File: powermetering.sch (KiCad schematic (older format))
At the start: 111 parts, among them J1 Conn_01x04, J2 Conn_01x02, J3 Conn_01x02, J4 Conn_01x02, J5 Conn_01x02, U1 ADuM7641, U2 ADE9000, Y1 Crystal

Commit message: repair schematic, change pcb outline to spelsberg tk1111
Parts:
- removed U1: ADuM7641, Housings_SSOP:QSOP-24_3.9x8.7mm_Pitch0.635mm, symbol analog_devices:ADuM7641
- added T1: Transformer_1P_1S, Transformer_THT:Transformer_CHK_EI30-2VA_1xSec, symbol Device:Transformer_1P_1S
- C1, C10, C11, C12, C13, C14, C15, C16, C17, C18, C19, C2, C20, C21, C22, C23, C24, C25, C26, C27, C28, C29, C3, C30, C31, C32, C33, C34, C4, C5, C6, C7, C8, C9: symbol device:C -> stmbl:C
- D1: symbol device:LED -> stmbl:LED
- D10, D11, D12, D13, D14, D15, D16, D17, D2, D3, D4, D5, D6, D7, D8, D9: symbol device:D -> stmbl:D
- F1, F2, F3, F4: symbol device:Fuse -> Device:Fuse
- J1: symbol Connector:Conn_01x04 -> Connector:Conn_01x04_Female
- J2, J3, J4, J5: symbol Connector:Conn_01x02 -> Connector:Conn_01x02_Female
- L1, L2, L3, L4: symbol device:Ferrite_Bead -> Device:Ferrite_Bead
- Y1: symbol device:Crystal -> stmbl:Crystal
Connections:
- net labels added: AVDDOUT, DVDDOUT, IL1N, IL1P, IL2N, IL2P, IL3N, IL3P, INN, INP, REF, UL1N, UL1P, UL2N, UL2P, UL3N, UL3P

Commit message: add stm32, ethernet phy, hv supply with lnk304
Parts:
- added C35, C36: 3.9µ, Capacitor_SMD:CP_Elec_8x10, symbol stmbl:CP
- added C? (x2): 150n, stmbl:C_1808, symbol stmbl:C
- added D18, D19: ABS2, Diode_SMD:Diode_Bridge_Diotec_ABS, symbol Diode_Bridge:ABS2
- added D20, D21: ABS10, Diode_SMD:Diode_Bridge_Diotec_ABS, symbol Diode_Bridge:ABS10
- added D22: 1.5KExxA, Diode_THT:D_DO-201AE_P15.24mm_Horizontal, symbol Diode:1.5KExxA
- added H1, H2, H3, H4, H5, H6, H7, H8: MountingHole_Pad, MountingHole:MountingHole_3.2mm_M3_DIN965_Pad, symbol Mechanical:MountingHole_Pad
- added R45, R46: 450k, stmbl:R_1206, symbol stmbl:R
- added RV1: Varistor, symbol Device:Varistor
- added T2, T3: Transformer_1P_1S, Transformer_THT:Transformer_CHK_EI30-2VA_1xSec, symbol powermetering:Transformer_1P_1S
- F1, F2, F3, F4: footprint Fuse_Holders_and_Fuses:Fuseholder6x32_Horiz_Open_Schurter0031-8002 -> Fuse:Fuse_2920_7451Metric
- R1, R10, R11, R12, R13, R14, R15, R16, R17, R18, R19, R2, R20, R21, R22, R23, R24, R3, R4, R5, R6, R7, R8, R9: footprint Resistors_SMD:R_0603 -> stmbl:R_0603
- R25, R26, R27, R28, R29, R30, R31, R32, R33, R34, R35, R36, R37, R38, R39, R40, R41, R42, R43, R44: footprint Resistors_SMD:R_2010 -> Resistor_SMD:R_2010_5025Metric
- T1: symbol Device:Transformer_1P_1S -> powermetering:Transformer_1P_1S
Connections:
- net labels added: DC+, DC-, GNDPWR, VPP
- wire segments 356 -> 442
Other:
- moved on the sheet: F1, F2, F3, F4, J1, L4

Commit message: remove xfmrs from top board, no space with 18650 backup battery
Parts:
- added BT1: Battery_Cell, Battery:BatteryHolder_Keystone_1042_1x18650, symbol Device:Battery_Cell
- added H10, H11, H12, H13, H14, H15, H16, H9: MountingHole, MountingHole:MountingHole_3.2mm_M3, symbol Mechanical:MountingHole
- gave numbers to parts that had none: 2
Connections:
- net labels added: RESET
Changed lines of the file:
@@
 Wire Wire Line
 	3050 7050 3150 7050
-Text GLabel 15100 2300 2    50   Input ~ 0
+Text GLabel 15100 4400 2    50   Input ~ 0
 L1
 $Comp
@@
 	0    1    1    0
 $EndComp
-Text GLabel 15100 4400 2    50   Input ~ 0
+Text GLabel 15100 2300 2    50   Input ~ 0
 L3
 $Comp
@@
 $EndComp
 Text Label 12550 2550 0    50   ~ 0
-UL1N
+UL3N
 Text Label 13100 2550 0    50   ~ 0
-UL1P
+UL3P
 Text Label 13100 3400 0    50   ~ 0
 UL2P
 Text Label 13100 4300 0    50   ~ 0
-UL3P
+UL1P
 Text Label 12550 3450 0    50   ~ 0
 UL2N
 Text Label 12550 4350 0    50   ~ 0
-UL3N
+UL1N
 Connection ~ 12550 5850
 Wire Wire Line
@@
 	5000 4000 5100 4000
 $Comp
-L stmbl:C C?
+L stmbl:C C63
 U 1 1 5DA79E78
 P 4100 3450
-F 0 "C?" H 4150 3550 50  0000 L CNN
+F 0 "C63" H 4150 3550 50  0000 L CNN
 F 1 "150n" H 4150 3350 50  0000 L CNN
 F 2 "stmbl:C_1808" H 4138 3300 50  0001 C CNN
@@
 	4100 3300 4400 3300
 $Comp
-L stmbl:C C?
+L stmbl:C C73
 U 1 1 5DA7A654
 P 4100 3850
-F 0 "C?" H 4150 3950 50  0000 L CNN
+F 0 "C73" H 4150 3950 50  0000 L CNN
 F 1 "150n" H 4150 3750 50  0000 L CNN
 F 2 "stmbl:C_1808" H 4138 3700 50  0001 C CNN
@@
 Wire Wire Line
 	4100 3650 4100 3700
+Text Label 8400 6800 0    50   ~ 0
+RESET
+$Comp
+L Mechanical:MountingHole H9
+U 1 1 5DBB8804
+P 4500 7850
+F 0 "H9" H 4600 7896 50  0000 L CNN
+F 1 "MountingHole" H 4600 7805 50  0000 L CNN
+F 2 "MountingHole:MountingHole_3.2mm_M3" H 4500 7850 50  0001 C CNN
+F 3 "~" H 4500 7850 50  0001 C CNN
+	1    4500 7850
+	1    0    0    -1
+$EndComp
+$Comp
+L Mechanical:MountingHole H10
+U 1 1 5DBBF11A
+P 4500 8100
+F 0 "H10" H 4600 8146 50  0000 L CNN
+F 1 "MountingHole" H 4600 8055 50  0000 L CNN
+F 2 "MountingHole:MountingHole_3.2mm_M3" H 4500 8100 50  0001 C CNN
+F 3 "~" H 4500 8100 50  0001 C CNN
+	1    4500 8100
+	1    0    0    -1
+$EndComp
+$Comp
+L Mechanical:MountingHole H11
+U 1 1 5DBBF269
+P 4500 8350
+F 0 "H11" H 4600 8396 50  0000 L CNN
+F 1 "MountingHole" H 4600 8305 50  0000 L CNN
+F 2 "MountingHole:MountingHole_3.2mm_M3" H 4500 8350 50  0001 C CNN
+F 3 "~" H 4500 8350 50  0001 C CNN
+	1    4500 8350
+	1    0    0    -1
+$EndComp
+$Comp
+L Mechanical:MountingHole H12
+U 1 1 5DBBF7A6
+P 4500 8600
+F 0 "H12" H 4600 8646 50  0000 L CNN
+F 1 "MountingHole" H 4600 8555 50  0000 L CNN
+F 2 "MountingHole:MountingHole_3.2mm_M3" H 4500 8600 50  0001 C CNN
+F 3 "~" H 4500 8600 50  0001 C CNN
+	1    4500 8600
+	1    0    0    -1
+$EndComp
+$Comp
+L Mechanical:MountingHole H16
+U 1 1 5DBBF92B
+P 5300 8600
+F 0 "H16" H 5400 8646 50  0000 L CNN
+F 1 "MountingHole" H 5400 8555 50  0000 L CNN
+F 2 "MountingHole:MountingHole_3.2mm_M3" H 5300 8600 50  0001 C CNN
+F 3 "~" H 5300 8600 50  0001 C CNN
+	1    5300 8600
+	1    0    0    -1
+$EndComp
+$Comp
+L Mechanical:MountingHole H15
+U 1 1 5DBBFB1F
+P 5300 8350
+F 0 "H15" H 5400 8396 50  0000 L CNN
+F 1 "MountingHole" H 5400 8305 50  0000 L CNN
+F 2 "MountingHole:MountingHole_3.2mm_M3" H 5300 8350 50  0001 C CNN
+F 3 "~" H 5300 8350 50  0001 C CNN
+	1    5300 8350
+	1    0    0    -1
+$EndComp
+$Comp
+L Mechanical:MountingHole H14
+U 1 1 5DBBFF20
+P 5300 8100
+F 0 "H14" H 5400 8146 50  0000 L CNN
+F 1 "MountingHole" H 5400 8055 50  0000 L CNN
+F 2 "MountingHole:MountingHole_3.2mm_M3" H 5300 8100 50  0001 C CNN
+F 3 "~" H 5300 8100 50  0001 C CNN
+	1    5300 8100
+	1    0    0    -1
+$EndComp
+$Comp
+L Mechanical:MountingHole H13
+U 1 1 5DBC00A9
+P 5300 7850
+F 0 "H13" H 5400 7896 50  0000 L CNN
+F 1 "MountingHole" H 5400 7805 50  0000 L CNN
+F 2 "MountingHole:MountingHole_3.2mm_M3" H 5300 7850 50  0001 C CNN
+F 3 "~" H 5300 7850 50  0001 C CNN
+	1    5300 7850
+	1    0    0    -1
+$EndComp
+$Comp
+L Device:Battery_Cell BT1
+U 1 1 5DBD7F45
+P 1800 5750
+F 0 "BT1" H 1918 5846 50  0000 L CNN
+F 1 "Battery_Cell" H 1918 5755 50  0000 L CNN
+F 2 "Battery:BatteryHolder_Keystone_1042_1x18650" V 1800 5810 50  0001 C CNN
+F 3 "~" V 1800 5810 50  0001 C CNN
+	1    1800 5750
+	1    0    0    -1
+$EndComp
 $EndSCHEMATC

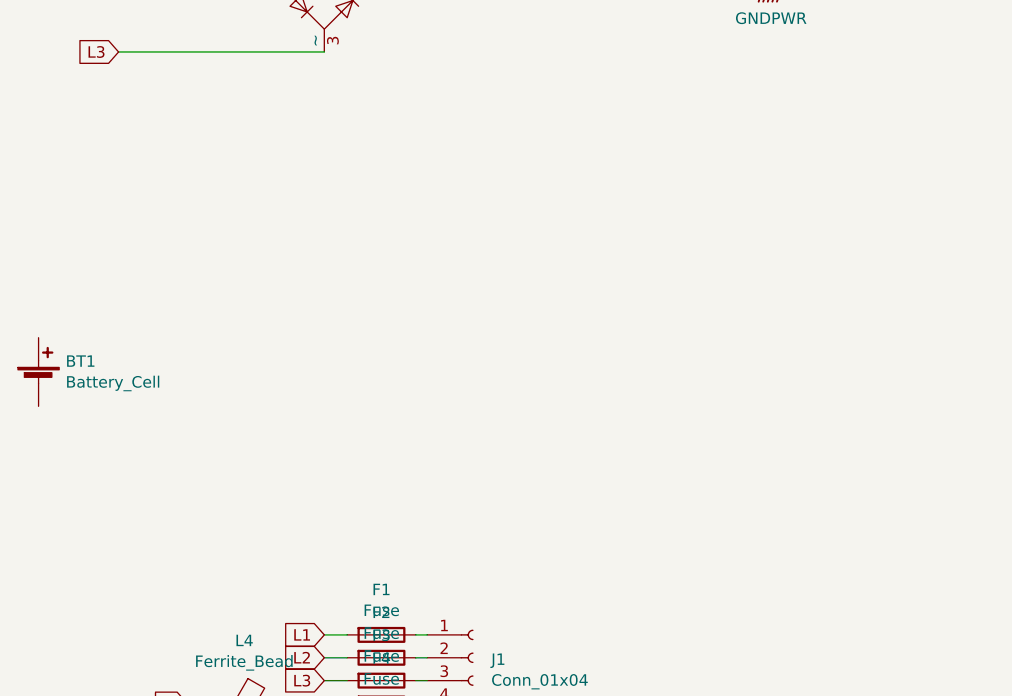
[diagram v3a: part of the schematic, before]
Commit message: start adding liion charger circuit
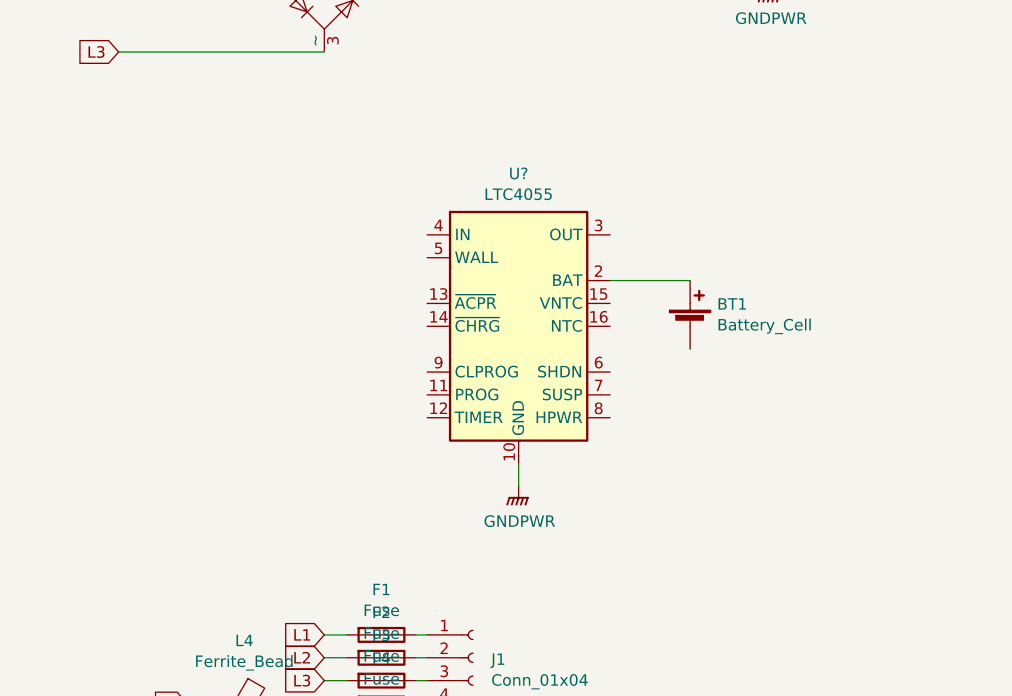
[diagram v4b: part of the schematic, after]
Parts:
- added U?: LTC4055, Package_DFN_QFN:QFN-16-1EP_4x4mm_P0.65mm_EP2.15x2.15mm, symbol Battery_Management:LTC4055
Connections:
- wire segments 442 -> 444
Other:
- moved on the sheet: BT1
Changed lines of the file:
@@
 L Device:Battery_Cell BT1
 U 1 1 5DBD7F45
-P 1800 5750
-F 0 "BT1" H 1918 5846 50  0000 L CNN
-F 1 "Battery_Cell" H 1918 5755 50  0000 L CNN
-F 2 "Battery:BatteryHolder_Keystone_1042_1x18650" V 1800 5810 50  0001 C CNN
-F 3 "~" V 1800 5810 50  0001 C CNN
-	1    1800 5750
+P 4650 5500
+F 0 "BT1" H 4768 5596 50  0000 L CNN
+F 1 "Battery_Cell" H 4768 5505 50  0000 L CNN
+F 2 "Battery:BatteryHolder_Keystone_1042_1x18650" V 4650 5560 50  0001 C CNN
+F 3 "~" V 4650 5560 50  0001 C CNN
+	1    4650 5500
 	1    0    0    -1
 $EndComp
+$Comp
+L Battery_Management:LTC4055 U?
+U 1 1 5DBFE5E8
+P 3900 5500
+F 0 "U?" H 3900 6167 50  0000 C CNN
+F 1 "LTC4055" H 3900 6076 50  0000 C CNN
+F 2 "Package_DFN_QFN:QFN-16-1EP_4x4mm_P0.65mm_EP2.15x2.15mm" H 3900 4600 50  0001 C CNN
+F 3 "https://www.analog.com/media/en/technical-documentation/data-sheets/4055fb.pdf" H 3900 5000 50  0001 C CNN
+	1    3900 5500
+	1    0    0    -1
+$EndComp
+Wire Wire Line
+	4300 5300 4650 5300
+$Comp
+L stmbl:GNDPWR #PWR?
+U 1 1 5DC40D57
+P 3900 6200
+F 0 "#PWR?" H 3900 6000 50  0001 C CNN
+F 1 "GNDPWR" H 3904 6046 50  0000 C CNN
+F 2 "" H 3900 6150 50  0001 C CNN
+F 3 "" H 3900 6150 50  0001 C CNN
+	1    3900 6200
+	1    0    0    -1
+$EndComp
+Wire Wire Line
+	3900 6100 3900 6200
 $EndSCHEMATC

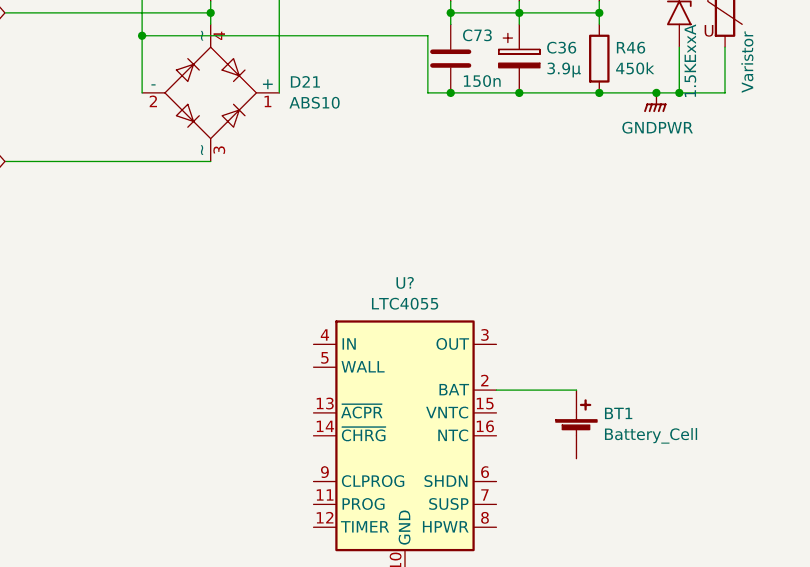
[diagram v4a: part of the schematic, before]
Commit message: add some 3d models
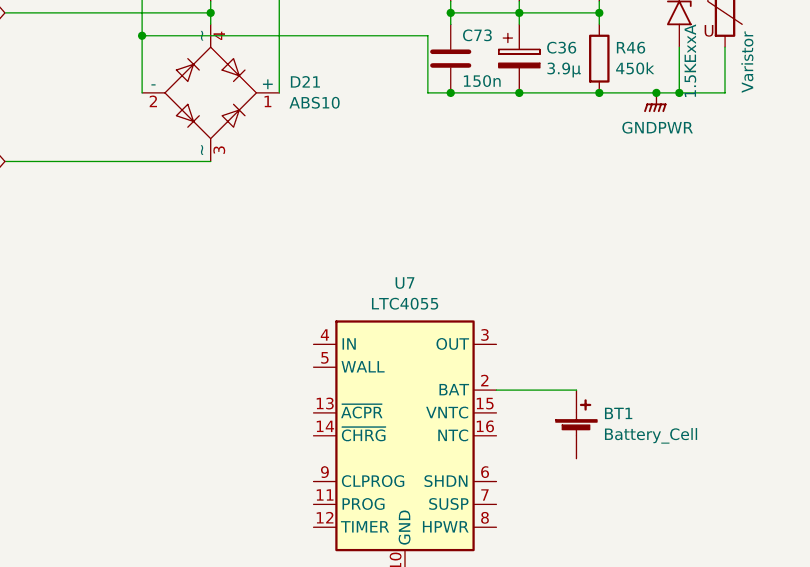
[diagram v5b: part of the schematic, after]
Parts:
- gave numbers to parts that had none: 1
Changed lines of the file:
@@
 $EndComp
 $Comp
-L Battery_Management:LTC4055 U?
+L Battery_Management:LTC4055 U7
 U 1 1 5DBFE5E8
 P 3900 5500
-F 0 "U?" H 3900 6167 50  0000 C CNN
+F 0 "U7" H 3900 6167 50  0000 C CNN
 F 1 "LTC4055" H 3900 6076 50  0000 C CNN
 F 2 "Package_DFN_QFN:QFN-16-1EP_4x4mm_P0.65mm_EP2.15x2.15mm" H 3900 4600 50  0001 C CNN
@@
 	4300 5300 4650 5300
 $Comp
-L stmbl:GNDPWR #PWR?
+L stmbl:GNDPWR #PWR0153
 U 1 1 5DC40D57
 P 3900 6200
-F 0 "#PWR?" H 3900 6000 50  0001 C CNN
+F 0 "#PWR0153" H 3900 6000 50  0001 C CNN
 F 1 "GNDPWR" H 3904 6046 50  0000 C CNN
 F 2 "" H 3900 6150 50  0001 C CNN
